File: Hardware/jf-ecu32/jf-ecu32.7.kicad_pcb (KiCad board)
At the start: 2 copper layers, 71.3 x 48 mm, 88 parts, among them J1 GAZ, J10 k, J11 RPM, J12 S.PORT, J13 PPM/PWM, J14 PUMP1, J15 PUMP1, J16 PPM/PWM, J17 PUMP2, J18 PUMP2, J19 EN, J2 AUX, J21 Conn_01x07, J3 PPM/PWM, J4 STARTER, J5 GLOW, J6 VANNE KEROSTART, J7 VANNE KERO, J8 BATTERY 2S/3S, J9 STARTER, Q1 AO3400A, Q2 QM6006D, Q3 AO3400A, Q4 QM6006D, Q5 QM6006D, Q6 QM6006D, Q7 AO3400A, Q8 AO3400A, U1 ESP32-WROOM-32D, U2 4050, U3 MAX31855KASA, U4 AMS1117-3.3, U5 4050, U6 AMS1117-5.0, U7 OPA340NA, U8 LM4040DBZ-2.5, U9 INA219AxDCN

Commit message: PCB + SRC
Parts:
- moved C11 0.38 mm to (34.4, 151.6)
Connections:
- net Net-(J13-Pin_3) renamed P1_OUTPUT
- net Net-(J16-Pin_3) renamed P2_OUTPUT
- net Net-(J3-Pin_3) renamed ST_OUTPUT
- U1 pad 33: RPM-2 -> ESP_SDA
- U1 pad 36: AUX -> ESP_SCL
- U1 pad 6: ESP_SDA -> RPM-2
- U1 pad 7: ESP_SCL -> AUX
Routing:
- net RPM-2: track 34.7 -> 54.9 mm, vias 1 -> 3
- net TX2: track 32.1 -> 40.8 mm
- net PPM_PWM_PUMP2_3.3: track 42.3 -> 33.8 mm
- net 3.3V: track 193.9 -> 202.2 mm
- net RPM: track 42.2 -> 35.9 mm
- net ESP_SCL: track 40.7 -> 46.7 mm
- net AUX: track 29.5 -> 35.0 mm, vias 1 -> 3
- net ESP_SDA: track 42.5 -> 47.1 mm
- net +5V: track 98.5 -> 94.1 mm
- net PPM_GAZ: track 33.7 -> 30.3 mm
- net IO0: track 22.5 -> 19.2 mm
- net OneWire: track 28.0 -> 25.2 mm, vias 3 -> 1
- net PPM_GAZ_5V: track 15.1 -> 15.8 mm
- net P1_OUTPUT: track 25.0 -> 24.4 mm
- net GND: vias 372 -> 355

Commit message: PCB
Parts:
- added R25: 100K, Resistor_SMD:R_0603_1608Metric, B.Cu at (39.6, 184.7)
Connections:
- Q7 pad 3: BR_MOSFET -> Net-(Q7-D)
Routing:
- net Net-(Q7-D): track 0.00 -> 1.88 mm
- net GND: vias 355 -> 354

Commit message: pcb
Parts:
- removed R25: 100K, Resistor_SMD:R_0603_1608Metric
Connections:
- Q7 pad 3: Net-(Q7-D) -> BR_MOSFET
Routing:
- net Net-(Q7-D): track 1.88 -> 0.00 mm
- net BR_MOSFET: track 51.0 -> 51.7 mm
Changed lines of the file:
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@@
   (net 80 "GND")
   (net 81 "OneWire")
-  (net 82 "Net-(Q7-D)")
   (footprint "Connector_PinHeader_2.00mm:PinHeader_1x01_P2.00mm_Vertical" (layer "F.Cu")
     (at 47.371 163.068)
@@
     (property "ki_keywords" "R res resistor")
     (attr smd)
-    (fp_text reference "R1" (at -4.168 1.816 90) (layer "F.SilkS")
+    (fp_text reference "R1" (at -1.882 2.578 180) (layer "F.SilkS")
         (effects (font (size 1 1) (thickness 0.15)))
     )
@@
   )
   (footprint "Resistor_SMD:R_0603_1608Metric" (layer "B.Cu")
-    (at 39.561 184.658 180)
-    (descr "Resistor SMD 0603 (1608 Metric), square (rectangular) end terminal, IPC_7351 nominal, (Body size source: IPC-SM-782 page 72, https://www.pcb-3d.com/wordpress/wp-content/uploads/ipc-sm-782a_amendment_1_and_2.pdf), generated with kicad-footprint-generator")
-    (tags "resistor")
-    (property "Sheetfile" "jf-ecu32.7.kicad_sch")
-    (property "Sheetname" "")
-    (property "ki_description" "Resistor")
-    (property "ki_keywords" "R res resistor")
-    (attr smd)
-    (fp_text reference "R25" (at -2.857 0) (layer "B.SilkS")
-        (effects (font (size 1 1) (thickness 0.15)) (justify mirror))
-    )
-    (fp_text value "100K" (at 0 -1.43) (layer "B.Fab")
-        (effects (font (size 1 1) (thickness 0.15)) (justify mirror))
-    )
-    (fp_text user "${REFERENCE}" (at -0.063 0) (layer "B.Fab")
-        (effects (font (size 0.4 0.4) (thickness 0.06)) (justify mirror))
-    )
-    (fp_line (start -0.237258 -0.5225) (end 0.237258 -0.5225)
-      (stroke (width 0.12) (type solid)) (layer "B.SilkS"))
-    (fp_line (start -0.237258 0.5225) (end 0.237258 0.5225)
-      (stroke (width 0.12) (type solid)) (layer "B.SilkS"))
-    (fp_line (start -1.48 -0.73) (end -1.48 0.73)
-      (stroke (width 0.05) (type solid)) (layer "B.CrtYd"))
-    (fp_line (start -1.48 0.73) (end 1.48 0.73)
-      (stroke (width 0.05) (type solid)) (layer "B.CrtYd"))
-    (fp_line (start 1.48 -0.73) (end -1.48 -0.73)
-      (stroke (width 0.05) (type solid)) (layer "B.CrtYd"))
-    (fp_line (start 1.48 0.73) (end 1.48 -0.73)
-      (stroke (width 0.05) (type solid)) (layer "B.CrtYd"))
-    (fp_line (start -0.8 -0.4125) (end -0.8 0.4125)
-      (stroke (width 0.1) (type solid)) (layer "B.Fab"))
-    (fp_line (start -0.8 0.4125) (end 0.8 0.4125)
-      (stroke (width 0.1) (type solid)) (layer "B.Fab"))
-    (fp_line (start 0.8 -0.4125) (end -0.8 -0.4125)
-      (stroke (width 0.1) (type solid)) (layer "B.Fab"))
-    (fp_line (start 0.8 0.4125) (end 0.8 -0.4125)
-      (stroke (width 0.1) (type solid)) (layer "B.Fab"))
-    (pad "1" smd roundrect (at -0.825 0 180) (size 0.8 0.95) (layers "B.Cu" "B.Paste" "B.Mask") (roundrect_rratio 0.25)
-      (net 76 "BR_MOSFET") (pintype "passive"))
-    (pad "2" smd roundrect (at 0.825 0 180) (size 0.8 0.95) (layers "B.Cu" "B.Paste" "B.Mask") (roundrect_rratio 0.25)
-      (net 82 "Net-(Q7-D)") (pintype "passive"))
-    (model "${KICAD6_3DMODEL_DIR}/Resistor_SMD.3dshapes/R_0603_1608Metric.wrl"
-      (offset (xyz 0 0 0))
-      (scale (xyz 1 1 1))
-      (rotate (xyz 0 0 0))
-    )
-  )
-  (footprint "Resistor_SMD:R_0603_1608Metric" (layer "B.Cu")
     (at 46.19 190.825 90)
     (descr "Resistor SMD 0603 (1608 Metric), square (rectangular) end terminal, IPC_7351 nominal, (Body size source: IPC-SM-782 page 72, https://www.pcb-3d.com/wordpress/wp-content/uploads/ipc-sm-782a_amendment_1_and_2.pdf), generated with kicad-footprint-generator")
@@
       (net 80 "GND") (pinfunction "S") (pintype "passive"))
     (pad "3" smd roundrect (at 0.9375 0) (size 1.475 0.6) (layers "B.Cu" "B.Paste" "B.Mask") (roundrect_rratio 0.25)
-      (net 82 "Net-(Q7-D)") (pinfunction "D") (pintype "passive"))
+      (net 76 "BR_MOSFET") (pinfunction "D") (pintype "passive"))
     (model "${KICAD6_3DMODEL_DIR}/Package_TO_SOT_SMD.3dshapes/SOT-23.wrl"
       (offset (xyz 0 0 0))
@@
   (segment (start 41.22 185.3) (end 40.42 186.1) (width 0.25) (layer "B.Cu") (net 76))
   (segment (start 30.095 177.972) (end 29.995 177.872) (width 0.25) (layer "B.Cu") (net 76))
+  (segment (start 38.73 186.1) (end 40.42 186.1) (width 0.25) (layer "B.Cu") (net 76))
   (segment (start 31.115 181.442) (end 30.095 180.422) (width 0.25) (layer "B.Cu") (net 76))
-  (segment (start 40.386 184.658) (end 40.386 186.066) (width 0.25) (layer "B.Cu") (net 76))
   (segment (start 27.575 183.44) (end 30.712463 183.44) (width 0.25) (layer "B.Cu") (net 76))
   (segment (start 45.06 180.39) (end 45.06 182.873604) (width 0.25) (layer "B.Cu") (net 76))
   (segment (start 26.945 177.972) (end 26.06 177.087) (width 0.25) (layer "B.Cu") (net 76))
-  (segment (start 40.386 186.066) (end 40.42 186.1) (width 0.25) (layer "B.Cu") (net 76))
   (segment (start 46.081232 179.368768) (end 45.06 180.39) (width 0.25) (layer "B.Cu") (net 76))
+  (segment (start 38.42 186.41) (end 38.73 186.1) (width 0.25) (layer "B.Cu") (net 76))
   (segment (start 30.095 180.422) (end 30.095 177.972) (width 0.25) (layer "B.Cu") (net 76))
   (segment (start 27.971168 177.872) (end 27.871168 177.972) (width 0.25) (layer "B.Cu") (net 76))
@@
   (segment (start 75.087927 178.7481) (end 62.5281 178.7481) (width 0.25) (layer "B.Cu") (net 81))
   (segment (start 62.5281 178.7481) (end 59.47 175.69) (width 0.25) (layer "B.Cu") (net 81))
-  (segment (start 38.736 184.658) (end 38.42 184.974) (width 0.25) (layer "B.Cu") (net 82))
-  (segment (start 38.42 184.974) (end 38.42 186.41) (width 0.25) (layer "B.Cu") (net 82))
   (zone (net 80) (net_name "GND") (layers "F&B.Cu") (name "GND") (hatch edge 0.508)
     (connect_pads yes (clearance 0.2))

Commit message: Test Carte V3 - Maj vers V4
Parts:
- added Q9: FDD6685, Package_TO_SOT_SMD:TO-252-2, F.Cu at (31.6, 192.8)
- C1: moved to B.Cu
- D10, D13, D15, D3: value D_Schottky -> D_Schottky SS34
- D7, D9: value D_Schottky -> D_Schottky SS14
- Q1, Q3, Q7, Q8: value AO3400A -> A49T
- Q2, Q4, Q5, Q6: value QM6006D -> LR8726
- R10, R11, R12, R7, R8, R9: value R -> 10K
- moved Q2 21.3 mm to (13.5, 205.2)
- moved R11 2.00 mm to (36.6, 192.7), turned to 90 degrees
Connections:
- R11 pad 2: GND -> +BATT
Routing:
- net PWM_GLOW: track 59.3 -> 53.7 mm
- net +BATT: track 136.5 -> 141.6 mm, vias 17 -> 7
- net RPM: track 35.9 -> 32.7 mm
- net Net-(D10-K): track 24.4 -> 26.0 mm
- net VBAT_ADC: track 82.1 -> 82.7 mm, vias 0 -> 1
- removed copper zone on B.Cu, net +BATT
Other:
- board text added: "JF-ECU32 3.0 03-2025"
- board text removed: "JF-ECU32 3.0 09-2024"

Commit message: PCB V4 updated
PCB V4
File server
Glow current read
Voltage Read
Starter calibration working
Many links corrected
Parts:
- added D11: LED, LED_SMD:LED_0603_1608Metric, F.Cu at (57.1, 155.2)
- added D12: LED, LED_SMD:LED_0603_1608Metric, F.Cu at (30.6, 168.5)
- added D2: LED, LED_SMD:LED_0603_1608Metric, F.Cu at (36.6, 186.3)
- added D4: LED, LED_SMD:LED_0603_1608Metric, F.Cu at (36.6, 172.5)
- added D5: LED, LED_SMD:LED_0603_1608Metric, F.Cu at (30.7, 165.5)
- added D6: LED, LED_SMD:LED_0603_1608Metric, F.Cu at (44.5, 186.7)
- added D8: LED, LED_SMD:LED_0603_1608Metric, F.Cu at (70.6, 151.1)
- added R25: 10K, Resistor_SMD:R_0603_1608Metric, F.Cu at (46.2, 186.7)
- added R32: 10K, Resistor_SMD:R_0603_1608Metric, F.Cu at (67.2, 151.1)
- added R33: 10K, Resistor_SMD:R_0603_1608Metric, F.Cu at (57.1, 152.1)
- Q2: value LR8726 -> A49T; footprint Package_TO_SOT_SMD:TO-252-2 -> Package_TO_SOT_SMD:SOT-23
- moved Q2 33.9 mm to (42.0, 187.0), turned to -90 degrees
- moved R12 3.88 mm to (33.6, 165.5), turned to 180 degrees
- moved R10 3.79 mm to (33.5, 168.5), turned to 0 degrees
- moved R7 2.03 mm to (38.6, 186.3), turned to -90 degrees
- moved R8 1.67 mm to (38.2, 172.5), turned to -90 degrees
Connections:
- Q2 pad 2: +BATT -> GND
- Q2 pad 3: Net-(D10-K) -> Net-(Q2-D)
- Q9 pad 1: PWM_GLOW -> Net-(Q2-D)
- R10 pad 1: PWM_KEROSTART -> Net-(D12-K)
- R11 pad 1: PWM_GLOW -> Net-(Q2-D)
- R12 pad 1: PWM_KERO -> GND
- R12 pad 2: GND -> Net-(D5-K)
- R7 pad 1: P1_MOSFET -> Net-(D2-K)
- R8 pad 1: P2_MOSFET -> Net-(D4-K)
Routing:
- net PWM_GLOW: track 53.7 -> 42.2 mm
- net Net-(Q2-D): track 0.00 -> 10.6 mm
- net P1_MOSFET: track 30.5 -> 26.8 mm
- net Net-(D2-K): track 0.00 -> 2.05 mm
- net 3.3V: track 202.2 -> 204.1 mm
- net Net-(D6-K): track 0.00 -> 1.79 mm
- net Net-(D8-K): track 0.00 -> 1.73 mm
- net Net-(D4-K): track 0.00 -> 1.67 mm
- net Net-(D11-K): track 0.00 -> 1.44 mm
- net Net-(D12-K): track 0.00 -> 1.31 mm
- net Net-(D5-K): track 0.00 -> 1.24 mm
- net PWM_KEROSTART: track 37.1 -> 36.6 mm
- net GND: track 0.30 -> 0.59 mm, vias 354 -> 362
- net +5V: vias 10 -> 11
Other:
- board text added: "JF-ECU32 4.0 04-2025"
- board text removed: "JF-ECU32 3.0 03-2025"

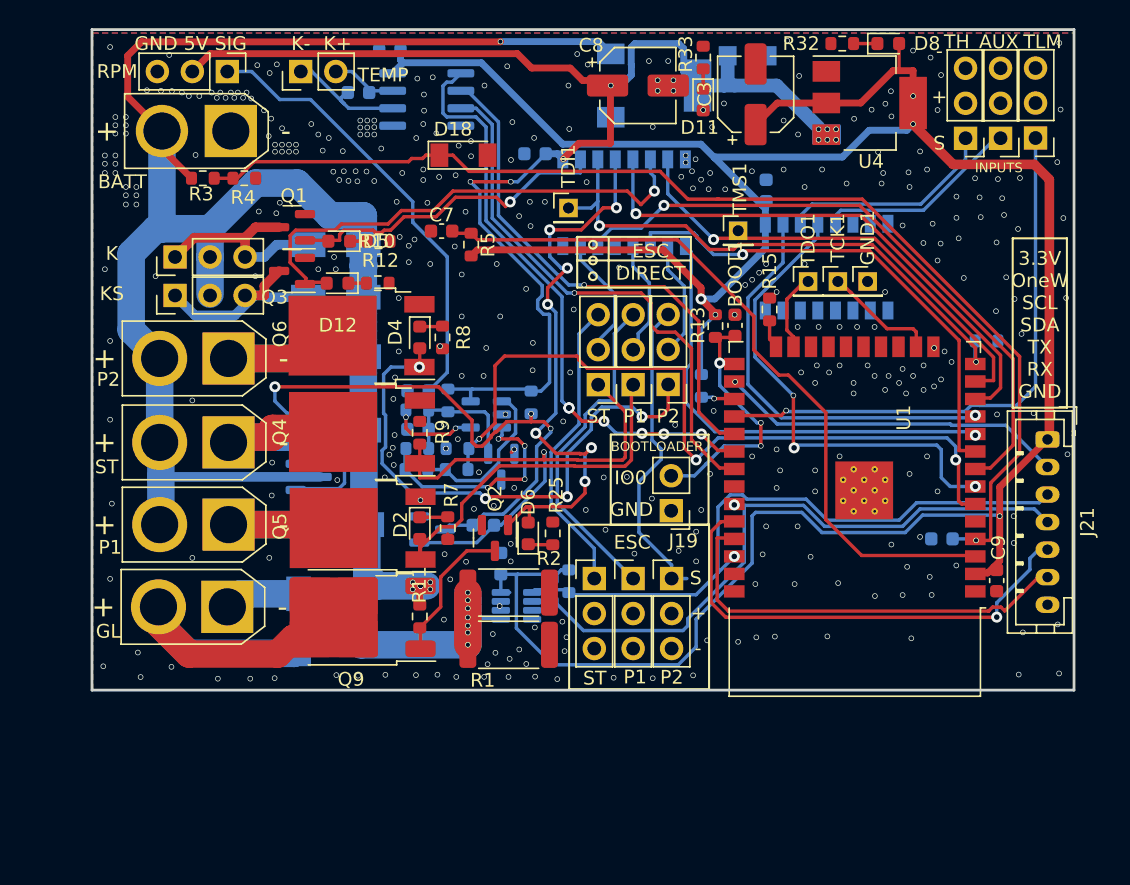
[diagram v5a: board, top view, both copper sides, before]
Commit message: Added MicroSD and BMP280
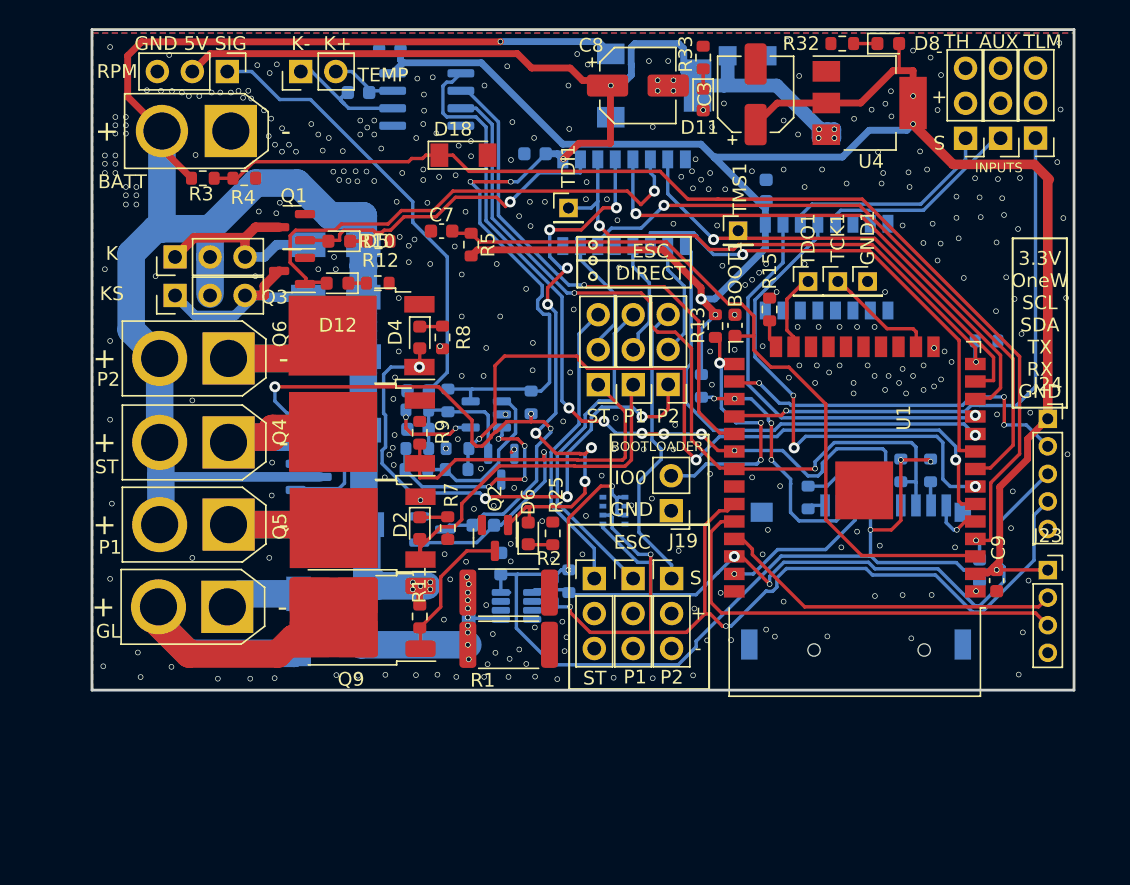
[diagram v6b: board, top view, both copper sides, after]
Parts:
- removed J21: Conn_01x07, Connector_JST:JST_PH_B7B-PH-K_1x07_P2.00mm_Vertical
- added J22: Micro_SD_Card_Det1, Connector_Card:J_SD_Card-micro_socket_A, B.Cu at (69.2, 191.7)
- added J23: Conn_01x04, Connector_PinSocket_2.00mm:PinSocket_1x04_P2.00mm_Vertical, F.Cu at (82.2, 189.4)
- added J24: Conn_01x05, Connector_PinSocket_2.00mm:PinSocket_1x05_P2.00mm_Vertical, F.Cu at (82.2, 178.4)
- added R26: 10K, Resistor_SMD:R_0603_1608Metric, B.Cu at (64.8, 184.1)
- added R27: 10K, Resistor_SMD:R_0603_1608Metric, B.Cu at (73.7, 182.1)
- added R28: 10K, Resistor_SMD:R_0603_1608Metric, B.Cu at (71.5, 182.1)
- added R29: 10K, Resistor_SMD:R_0603_1608Metric, B.Cu at (68.7, 182.8)
- added U10: BMP280, Package_LGA:Bosch_LGA-8_2x2.5mm_P0.65mm_ClockwisePinNumbering, B.Cu at (50.7, 185.0)
- moved C1 3.55 mm to (77.2, 189.4), turned to -90 degrees
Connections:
- net CS renamed CS_MAX31855
- net Net-(U1-IO16) renamed SD_CS
- BOOT1 pad 1: IO0 -> Net-(U1-EN)
- U1 pad 5: unconnected-(U1-SENSOR_VN-Pad5) -> SD_DET
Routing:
- net 3.3V: track 204.1 -> 234.3 mm, vias 5 -> 10
- net ESP_SDA: track 47.1 -> 68.2 mm, vias 1 -> 3
- net MISO: track 39.5 -> 59.3 mm, vias 1 -> 2
- net CLK: track 43.4 -> 60.4 mm
- net SD_CS: track 2.69 -> 18.3 mm, vias 1 -> 4
- net MOSI: track 0.00 -> 13.5 mm, vias 0 -> 1
- net ESP_SCL: track 46.7 -> 55.9 mm, vias 1 -> 2
- net TX: track 30.7 -> 25.3 mm
- net SD_DET: track 0.00 -> 3.83 mm, vias 0 -> 1
- net +5V: track 94.1 -> 97.9 mm, vias 11 -> 9
- net RX: track 34.5 -> 32.3 mm, vias 1 -> 0
- net Net-(U1-EN): track 53.7 -> 55.6 mm
- net Net-(J22-DAT1): track 0.00 -> 1.60 mm
- net Net-(D10-A): track 29.3 -> 27.9 mm, vias 7 -> 10
- net Net-(J22-DAT2): track 0.00 -> 1.33 mm
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
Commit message: PCB Update
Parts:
- removed BOOT1: BOOT, Capacitor_SMD:C_0603_1608Metric
- added C14: 0.1µF, Capacitor_SMD:C_0603_1608Metric, F.Cu at (49.7, 184.3)
- J23: footprint Connector_PinSocket_2.00mm:PinSocket_1x04_P2.00mm_Vertical -> Connector_JST:JST_PH_B4B-PH-K_1x04_P2.00mm_Vertical
- J24: footprint Connector_PinSocket_2.00mm:PinSocket_1x05_P2.00mm_Vertical -> Connector_JST:JST_PH_B5B-PH-K_1x05_P2.00mm_Vertical
- moved C7 20.3 mm to (58.2, 168.0)
- moved R5 19.9 mm to (59.8, 169.4), turned to 0 degrees
- moved J24 1.59 mm to (82.3, 176.8), turned to -90 degrees
- moved R26 1.00 mm to (65.3, 183.3), turned to 0 degrees
- moved R15 0.38 mm to (62.4, 170.4)
- moved J23 0.18 mm to (82.3, 189.2), turned to -90 degrees
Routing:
- net Net-(U1-EN): track 55.6 -> 35.0 mm
- net 3.3V: track 234.3 -> 215.0 mm, vias 10 -> 9
- net ESP_SCL: track 55.9 -> 57.5 mm
- net ESP_SDA: track 68.2 -> 69.8 mm
- net Net-(J22-DAT2): track 1.33 -> 2.06 mm
- net OneWire: track 26.4 -> 25.9 mm
- net GND: vias 349 -> 347
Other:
- board text added: "3.3V"
- board text added: "3.3V OneW SCL SDA GND"
- board text added: "3.3V TX RX GND"
- board text added: "5V"
- board text added: "RX INPUTS"
- board text removed: "3.3V OneW SCL SDA TX RX GND"
- board text removed: "INPUTS"
- board text removed: "S + -"

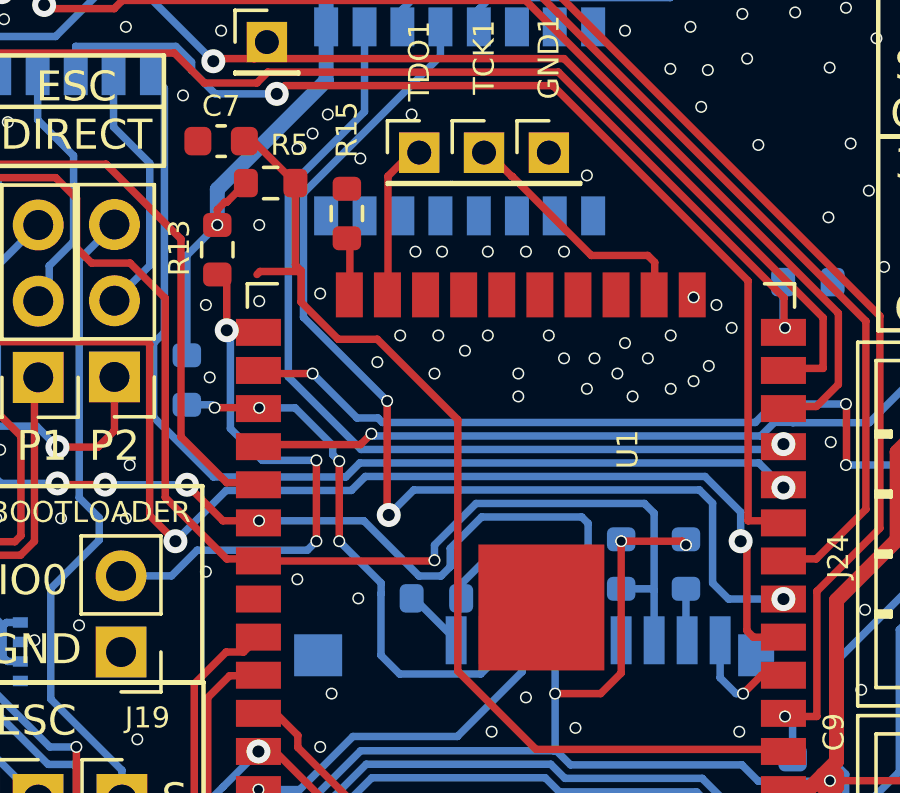
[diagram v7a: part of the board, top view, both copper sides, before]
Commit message: Logs moved to SDCard
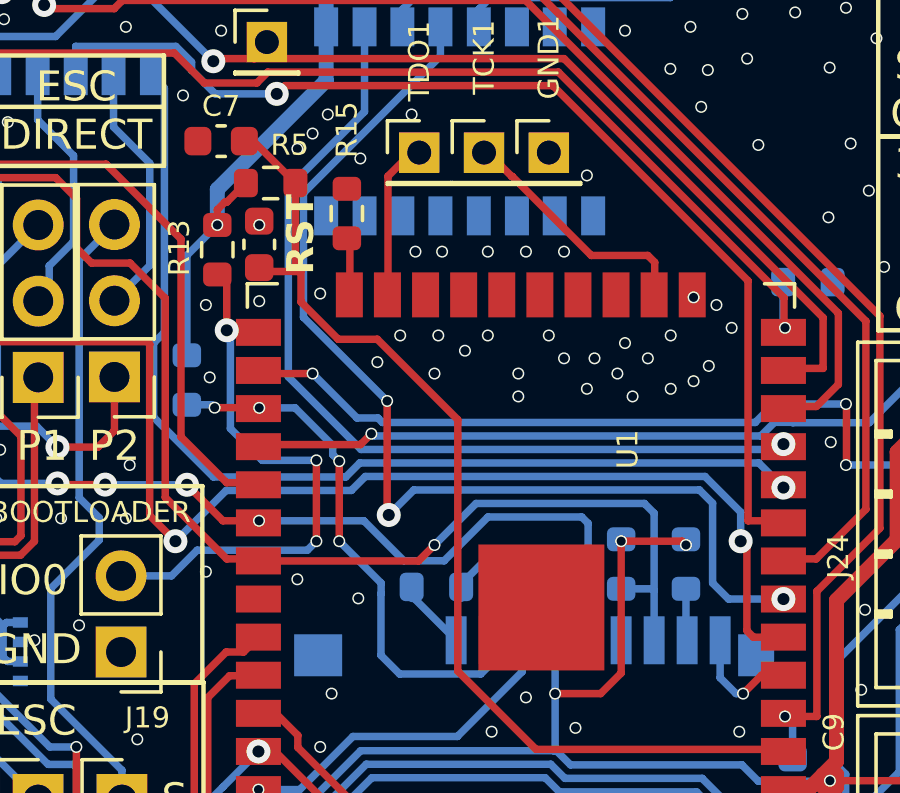
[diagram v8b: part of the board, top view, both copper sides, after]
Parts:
- added RST1: BOOT, Capacitor_SMD:C_0603_1608Metric, F.Cu at (59.4, 171.5)
- moved R26 0.38 mm to (65.3, 182.9)
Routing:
- net CLK: track 60.4 -> 59.6 mm
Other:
- board text added: "RST"
